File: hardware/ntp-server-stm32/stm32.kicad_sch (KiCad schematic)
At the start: 35 parts, among them Q6 BC847W, Q7 BC847W, U12 STM32H563VIT6, U13 LT3045xDD, U14 MCP1502T-33E/CHY, Y2 32.768kHz

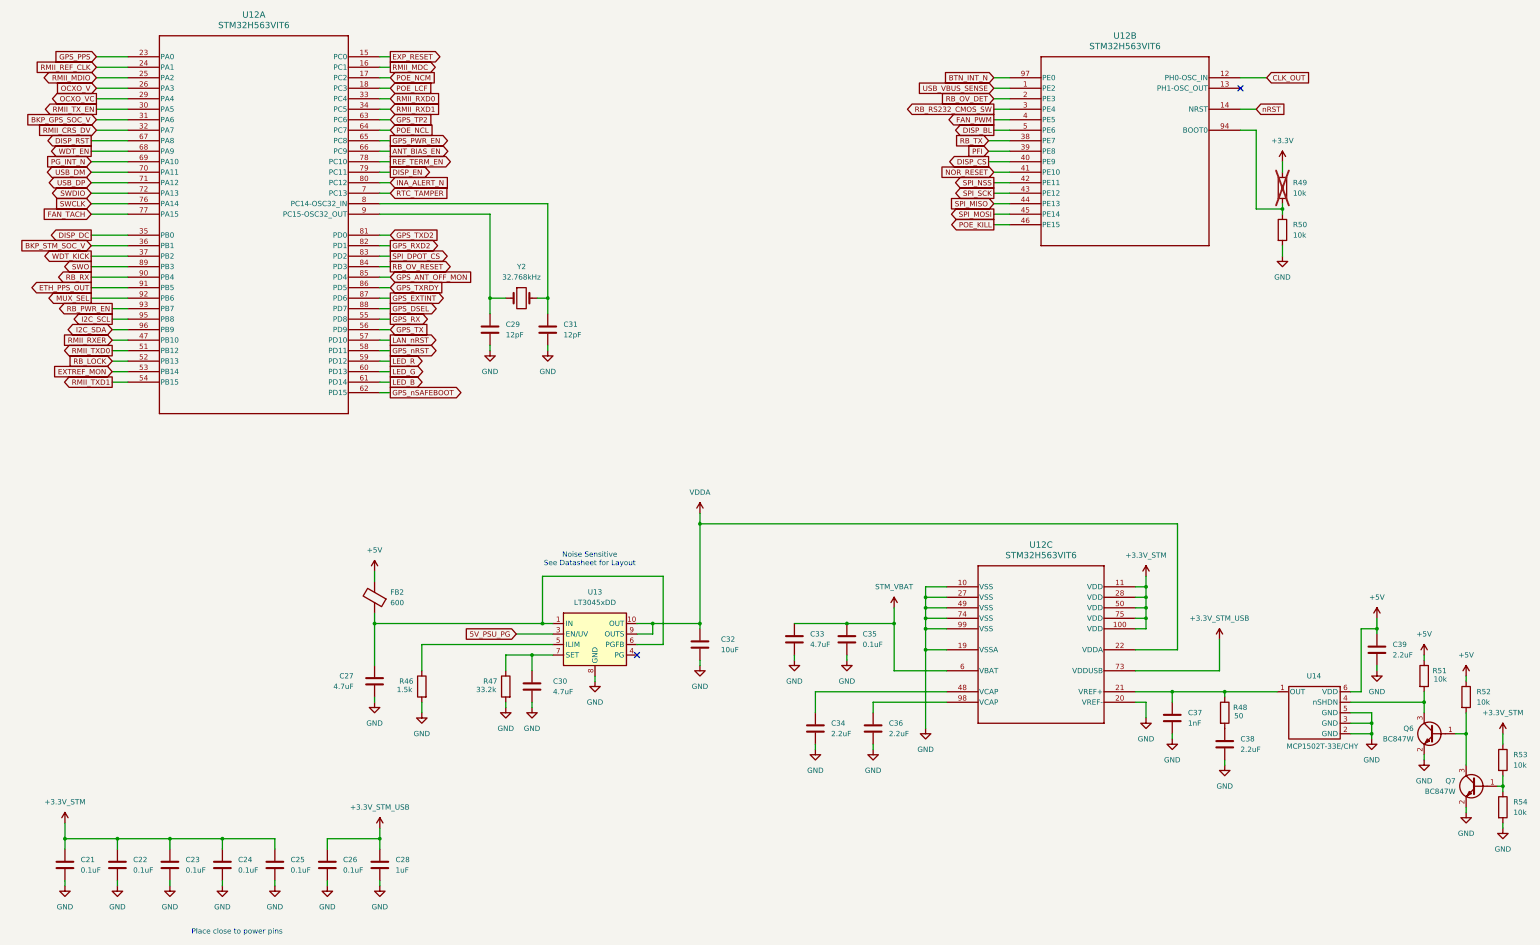
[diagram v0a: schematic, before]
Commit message: Standardize net/rail names: plain 3V3 style, _N active-low, voltage-format PG/alerts
22 net renames applied across all sheets and verified: removed/added net-name
sets match intent exactly and all node connectivity is preserved (kicad-cli
netlist re-parse).

Co-Authored-By: Claude Opus 4.8 (1M context) <noreply@anthropic.com>
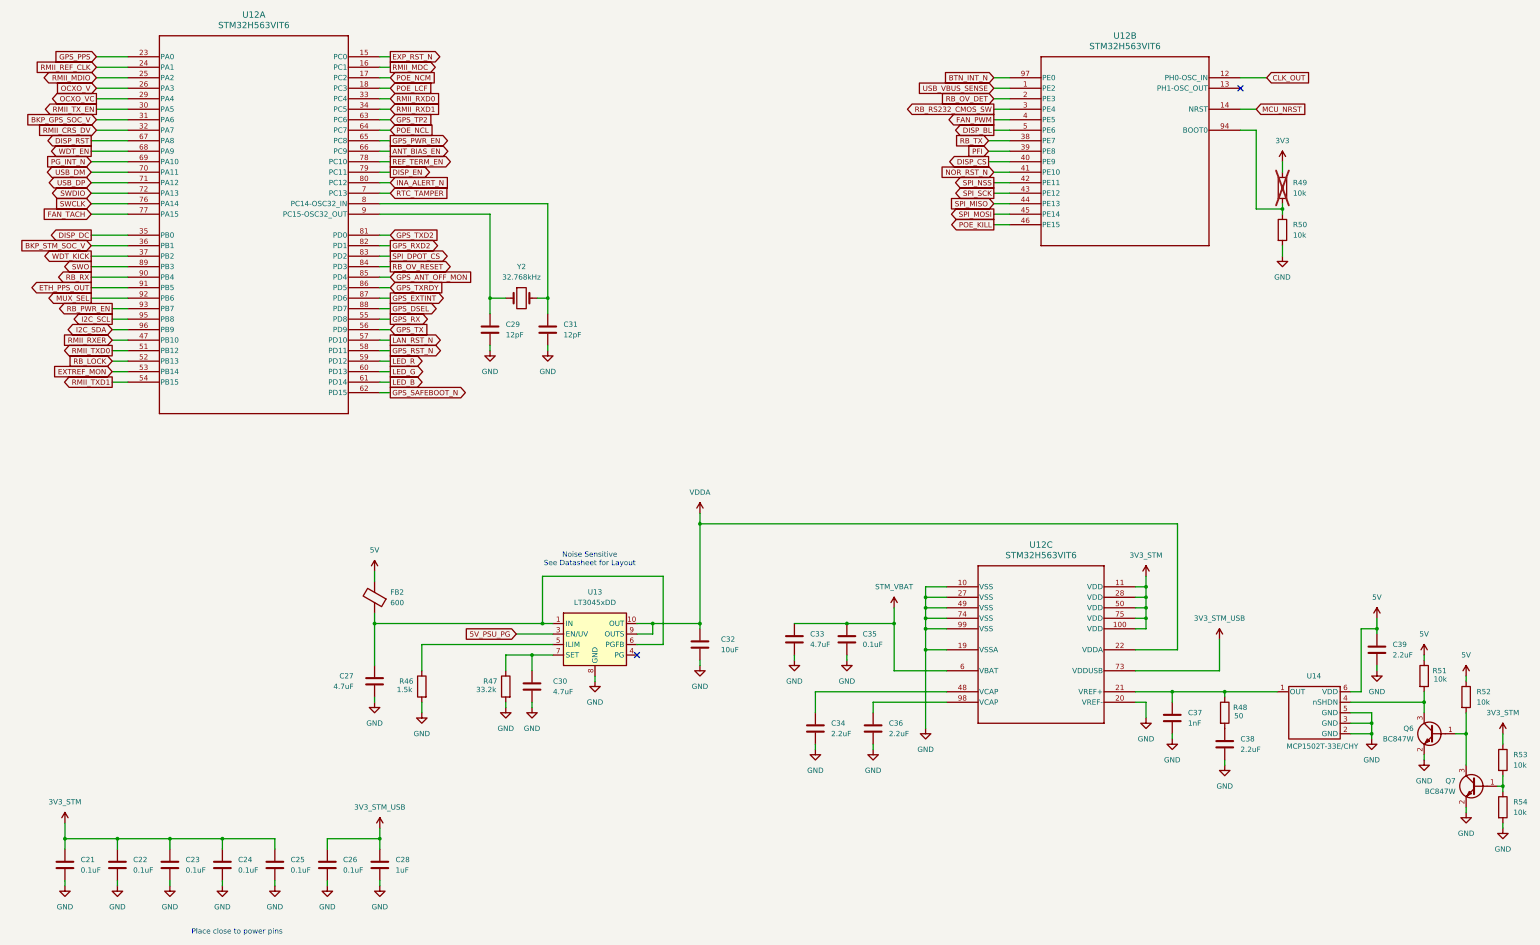
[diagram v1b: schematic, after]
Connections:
- net +3.3V renamed 3V3
- net +3.3V_STM renamed 3V3_STM
- net +3.3V_STM_USB renamed 3V3_STM_USB
- net +5V renamed 5V
- net EXP_RESET renamed EXP_RST_N
- net GPS_nRST renamed GPS_RST_N
- net GPS_nSAFEBOOT renamed GPS_SAFEBOOT_N
- net LAN_nRST renamed LAN_RST_N
- net NOR_RESET renamed NOR_RST_N
- net nRST renamed MCU_NRST
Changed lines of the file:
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@@
 		)
 	)
-	(global_label "EXP_RESET"
+	(global_label "EXP_RST_N"
 		(shape output)
 		(at 129.54 38.1 0)
@@
 		)
 	)
-	(global_label "GPS_nSAFEBOOT"
+	(global_label "GPS_SAFEBOOT_N"
 		(shape output)
 		(at 129.54 119.38 0)
@@
 		)
 	)
-	(global_label "NOR_RESET"
+	(global_label "NOR_RST_N"
 		(shape input)
 		(at 275.59 66.04 180)
@@
 		)
 	)
-	(global_label "GPS_nRST"
+	(global_label "GPS_RST_N"
 		(shape output)
 		(at 129.54 109.22 0)
@@
 		)
 	)
-	(global_label "nRST"
+	(global_label "MCU_NRST"
 		(shape input)
 		(at 339.09 50.8 0)
@@
 		)
 	)
-	(global_label "LAN_nRST"
+	(global_label "LAN_RST_N"
 		(shape output)
 		(at 129.54 106.68 0)
@@
 			)
 		)
-		(property "Value" "+3.3V_STM"
+		(property "Value" "3V3_STM"
 			(at 50.8 218.44 0)
 			(show_name no)
@@
 			)
 		)
-		(property "Value" "+3.3V_STM_USB"
+		(property "Value" "3V3_STM_USB"
 			(at 127 219.71 0)
 			(show_name no)
@@
 			)
 		)
-		(property "Value" "+5V"
+		(property "Value" "5V"
 			(at 368.3 168.91 0)
 			(show_name no)
@@
 			)
 		)
-		(property "Value" "+5V"
+		(property "Value" "5V"
 			(at 125.73 157.48 0)
 			(show_name no)
@@
 			)
 		)
-		(property "Value" "+3.3V_STM_USB"
+		(property "Value" "3V3_STM_USB"
 			(at 330.2 173.99 0)
 			(show_name no)
@@
 			)
 		)
-		(property "Value" "+5V"
+		(property "Value" "5V"
 			(at 379.73 177.8 0)
 			(show_name no)
@@
 			)
 		)
-		(property "Value" "+3.3V"
+		(property "Value" "3V3"
 			(at 345.44 58.42 0)
 			(show_name no)
@@
 			)
 		)
-		(property "Value" "+3.3V_STM"
+		(property "Value" "3V3_STM"
 			(at 398.78 196.85 0)
 			(show_name no)
@@
 			)
 		)
-		(property "Value" "+5V"
+		(property "Value" "5V"
 			(at 389.89 182.88 0)
 			(show_name no)
@@
 			)
 		)
-		(property "Value" "+3.3V_STM"
+		(property "Value" "3V3_STM"
 			(at 312.42 158.75 0)
 			(show_name no)

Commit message: Standardize + complete BOM; write fields back into KiCad symbols
- New sts1000_bom.csv: rebuilt from authoritative Value field (source MPN/footprint/
  description were corrupted by copy-paste). 338 standardized, 78 MPN-from-value,
  50 kept, ~64 flagged (SELECT/REVIEW-HV/SHUNT-REVIEW) each with full spec.
- Resistors -> deterministic Panasonic ERJ-2RKF 0402 1% 1/10W (consolidated 1 part/value).
- Caps -> verified Murata GRM parts where value matches; clean spec + footprint otherwise.
- 1633 symbol field updates (Value/Footprint/Description/MPN/Mfr/Digikey) written to
  .kicad_sch; netlist re-parse confirms connectivity byte-identical.
- Add docs/sts1000_net_naming.md naming reference.

Co-Authored-By: Claude Opus 4.8 (1M context) <noreply@anthropic.com>
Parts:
- C21, C22, C23, C24, C25, C26, C35: footprint (none) -> C_0402_1005Metric; DIGIKEY_PART_NUMBER (none) -> 490-6328-2-ND; MANUFACTURER (none) -> Murata; MANUFACTURER_PART_NUMBER (none) -> GRM155R71C104KA88J
- C27: footprint 0805 -> C_0805_2012Metric; DIGIKEY_PART_NUMBER 445-5972-1-ND -> 490-GRM21BR71C475KE51KTR-ND; MANUFACTURER TDK -> Murata; MANUFACTURER_PART_NUMBER C2012X7R1E475K125AB -> GRM21BR71C475KE51K
- C28: footprint (none) -> C_0603_1608Metric
- C29, C31: footprint (none) -> C_0402_1005Metric
- C30, C33: footprint (none) -> C_0805_2012Metric; DIGIKEY_PART_NUMBER (none) -> 490-GRM21BR71C475KE51KTR-ND; MANUFACTURER (none) -> Murata; MANUFACTURER_PART_NUMBER (none) -> GRM21BR71C475KE51K
- C32: footprint 1206 -> C_0805_2012Metric; DIGIKEY_PART_NUMBER 445-7705-1-ND -> 490-GRM21BZ71C106KE15LTR-ND; MANUFACTURER TDK -> Murata; MANUFACTURER_PART_NUMBER C3216X7R1E106K160AB -> GRM21BZ71C106KE15L
- C34, C36, C38, C39: footprint (none) -> C_0603_1608Metric; DIGIKEY_PART_NUMBER (none) -> 490-GRM188Z71C225KE43DTR-ND; MANUFACTURER (none) -> Murata; MANUFACTURER_PART_NUMBER (none) -> GRM188Z71C225KE43D
- C37: footprint (none) -> C_0402_1005Metric; DIGIKEY_PART_NUMBER (none) -> 490-GRM1555C1H102FA01JTR-ND; MANUFACTURER (none) -> Murata; MANUFACTURER_PART_NUMBER (none) -> GRM1555C1H102FA01J
- Q6, Q7: MANUFACTURER_PART_NUMBER (none) -> BC847W
- R46: footprint (none) -> R_0402_1005Metric; MANUFACTURER (none) -> Panasonic; MANUFACTURER_PART_NUMBER (none) -> ERJ-2RKF1501X
- R47: footprint (none) -> R_0402_1005Metric; MANUFACTURER (none) -> Panasonic; MANUFACTURER_PART_NUMBER (none) -> ERJ-2RKF3322X
- R48: footprint (none) -> R_0402_1005Metric; MANUFACTURER (none) -> Panasonic; MANUFACTURER_PART_NUMBER (none) -> ERJ-2RKF50R0X
- R49, R50, R51, R52, R53, R54: footprint (none) -> R_0402_1005Metric; MANUFACTURER (none) -> Panasonic; MANUFACTURER_PART_NUMBER (none) -> ERJ-2RKF1002X
- U13: MANUFACTURER_PART_NUMBER (none) -> LT3045xDD
- U14: MANUFACTURER_PART_NUMBER (none) -> MCP1502T-33E/CHY
